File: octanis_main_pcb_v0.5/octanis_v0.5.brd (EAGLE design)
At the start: 80 x 45 mm, 78 parts, among them IC1 BME280, Q1 32.768kHz, Q2 32.768kHz, U3 DRV8836DSSR, U4 DRV8836DSSR, U5 DRV8836DSSR, U7 DRV8836DSSR

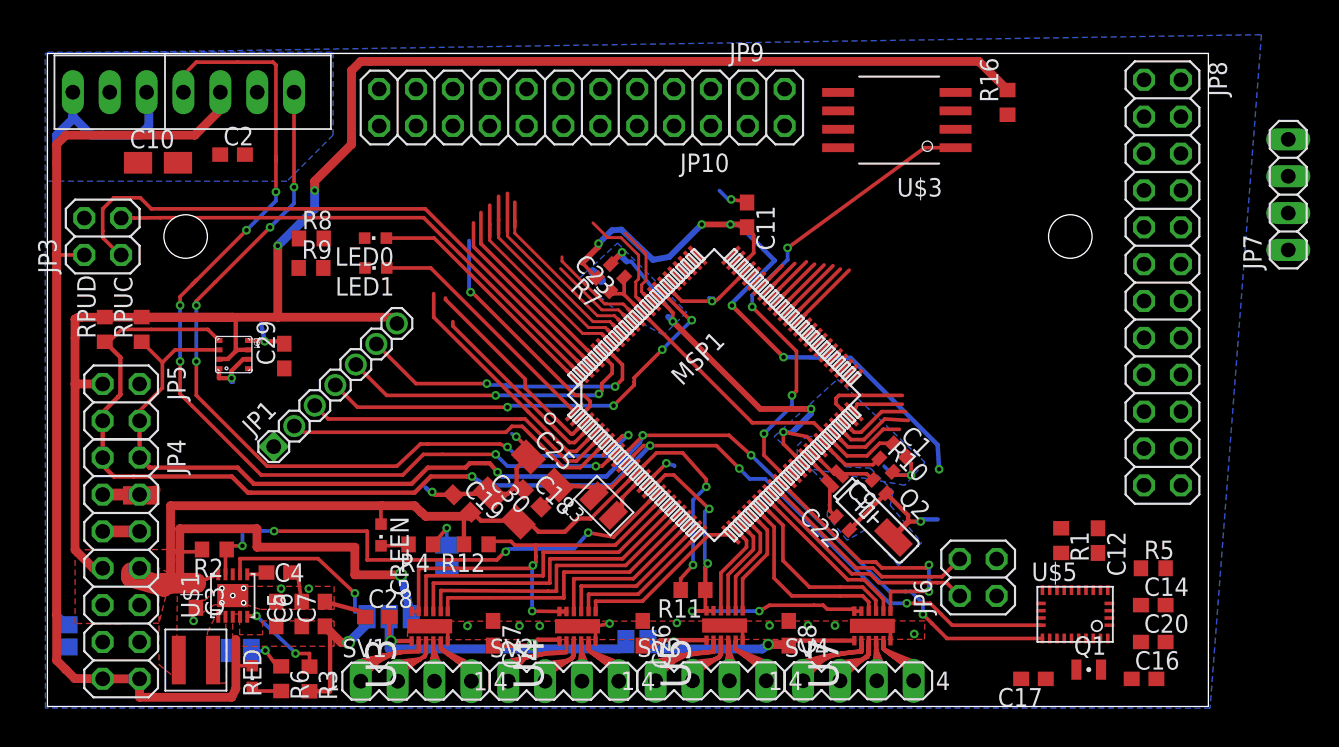
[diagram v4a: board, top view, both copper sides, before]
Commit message: mainboard: digital gpio routed
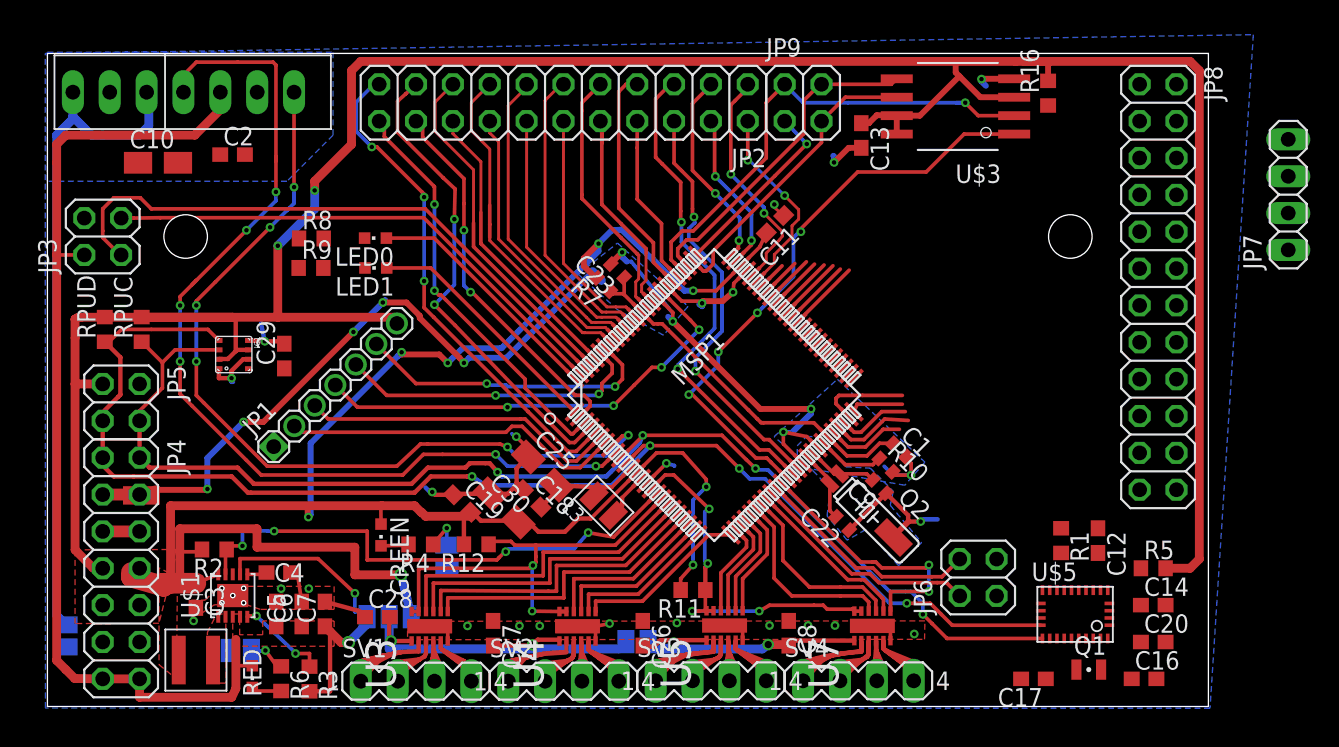
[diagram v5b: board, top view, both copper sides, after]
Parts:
- removed JP10: (no value), pinhead:2X10
- added C13: 100n, rcl:C0603
- added JP2: (no value), pinhead:2X11
- moved U$3 4.15 mm to (63.7, 41.3)
- moved R16 2.87 mm to (69.0, 42.3)
- moved JP9 2.56 mm to (52.1, 41.6)
- moved C11 2.03 mm to (50.1, 33.2), turned to 225 degrees
- moved JP8 0.43 mm to (76.5, 28.9)
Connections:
- removed net 3.3V: U$3.WP
- removed net N$15: JP10.2, MSP1.88
- removed net N$17: JP10.4, MSP1.89
- removed net N$20: JP10.6, MSP1.90
- removed net N$21: JP10.8, MSP1.91
- removed net P3.6/PM_UCB2SIMO/PM_UCB2SDA: MSP1.38
- removed net P3.7/PM_UCB2SOMI/PM_UCB2SCL: MSP1.39
- new net P3.6: JP2.5, MSP1.38
- new net P3.7: JP2.6, MSP1.39
- new net P7.0: JP2.12, MSP1.88
- new net P7.1: JP2.11, MSP1.89
- new net P7.2: JP2.14, MSP1.90
- new net P7.3: JP2.13, MSP1.91
- net +3V3: now also C13.1, U$3.WP
- net GND: now also C13.2
- net P1.0: now also JP2.19; no longer JP10.20
- net P1.1: now also JP2.21; no longer JP10.19
- net P10.2: now also JP2.20; no longer JP10.17
- net P10.3: now also JP2.22; no longer JP10.18
- net P5.6: now also JP2.2; no longer JP10.7
- net P5.7: now also JP2.1; no longer JP10.5
- net P6.6: now also JP2.8; no longer JP10.10
- net P6.7: now also JP2.7; no longer JP10.9
- net P9.2: now also JP2.4; no longer JP10.3
- net P9.3: now also JP2.3; no longer JP10.1
- net P9.4: now also JP2.18; no longer JP10.15
- net P9.5: now also JP2.17; no longer JP10.16
- net PJ.2: now also JP2.10; no longer JP10.13
- net PJ.3: now also JP2.9; no longer JP10.14
- net PJ.4: now also JP2.16; no longer JP10.11
- net PJ.5: now also JP2.15; no longer JP10.12
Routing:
- net +3V3: track 260.1 -> 331.1 mm, vias 11 -> 10
- net AGND: track 35.9 -> 77.4 mm, vias 5 -> 10
- net SPI_MISO: track 0.00 -> 34.3 mm, vias 0 -> 1
- net P3.6: track 0.00 -> 33.9 mm, vias 0 -> 2
- net P3.7: track 0.00 -> 29.9 mm, vias 0 -> 2
- net SPI_MOSI: track 0.00 -> 22.7 mm
- net P7.3: track 0.00 -> 21.6 mm
- net SPI_SCK: track 0.00 -> 20.7 mm
- net P7.1: track 0.00 -> 20.2 mm
- net P1.0: track 13.5 -> 33.1 mm, vias 0 -> 2
- net P7.2: track 0.00 -> 17.8 mm
- net P1.1: track 17.1 -> 34.8 mm, vias 0 -> 3
- net P7.0: track 0.00 -> 16.3 mm
- net P6.7: track 0.00 -> 16.0 mm
- net P5.7: track 0.00 -> 16.0 mm, vias 0 -> 2
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
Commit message: mainboard routing finished
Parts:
- removed JP7: SPI, pinhead:1X04
- moved C12 0.61 mm to (72.4, 10.8)
- moved R1 0.61 mm to (69.8, 10.8)
- moved R16 0.25 mm to (69.2, 42.3)
- moved C13 0.20 mm to (55.9, 39.3)
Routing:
- net +3V3: track 331.1 -> 369.3 mm
- net GND: track 72.2 -> 106.6 mm, vias 23 -> 32
- net A1: track 2.72 -> 34.1 mm
- net A0: track 1.99 -> 33.2 mm
- net A3: track 3.65 -> 33.1 mm
- net A9: track 0.00 -> 28.9 mm
- net A2: track 3.37 -> 30.3 mm
- net A8: track 0.00 -> 26.9 mm
- net A11: track 0.00 -> 26.8 mm
- net A5: track 4.47 -> 31.2 mm
- net A7: track 5.05 -> 31.2 mm
- net A13: track 0.00 -> 25.3 mm
- net A4: track 4.08 -> 28.9 mm
- net A17: track 0.00 -> 24.7 mm
- net A15: track 0.00 -> 24.7 mm
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
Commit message: mainboard finished
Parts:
- removed JP3: (no value), pinhead:2X02
- removed U$3: SST25VF064C, BertaLib:SOIC_8-LEAD
- added BLP, RST: PTR1B1,27, testpad:B1,27
- added RX3/TX3: (no value), pinhead:2X02
- added U6: DRV8836DSSR, DRV8834:SON50P200X300X80-13N
- U7: value DRV8836DSSR -> SST25VF064C; device DRV8834:SON50P200X300X80-13N -> BertaLib:SOIC_8-LEAD
- moved U7 36.4 mm to (63.7, 41.3)
- moved C11 1.15 mm to (50.0, 32.1)
- moved C2 0.57 mm to (12.7, 37.5)
- renumbered GREEN to 3V, JP1 to PROG, JP2 to DIGITAL_IO, JP6 to RX2/TX2, JP8 to ANALOG_IO, JP9 to SPI, L3 to L2, MSP1 to U1, RED to 5V, U$1 to U2, U$5 to IC2
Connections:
- removed net P5.6: DIGITAL_IO.2, U1.70
- removed net P5.7: DIGITAL_IO.1, U1.71
- net +3V3: now also DIGITAL_IO.1, RX2/TX2.3, RX3/TX3.3, U7.RST/HOLD, U7.VDD, U7.WP; no longer RX2/TX2.1, U$3.RST/HOLD, U$3.VDD, U$3.WP
- net +5V: no longer JP3.2
- net ACCEL_INT: now also U1.37
- net ACCEL_N_BOOTLD: now also BLP.TP
- net ACCEL_N_RST: now also RST.TP
- net GND: now also DIGITAL_IO.2, RX2/TX2.1, RX3/TX3.1, U1.71, U2.GND1, U2.GND2, U2.GND3, U2.GND4, U2.GND5, U6.13, U6.6, U7.VSS; no longer JP3.4, RX2/TX2.3, U$3.VSS, U7.13, U7.6
- net M5678SLEEP: now also U6.11, U6.12; no longer U7.11, U7.12
- net M7IN1: now also U6.10; no longer U7.10
- net M7IN2: now also U6.9; no longer U7.9
- net M8IN1: now also U6.8; no longer U7.8
- net M8IN2: now also U6.7; no longer U7.7
- net N$53: now also U6.2; no longer U7.2
- net N$54: now also U6.3; no longer U7.3
- net N$55: now also U6.4; no longer U7.4
- net N$56: now also U6.5; no longer U7.5
- net RX3: now also RX3/TX3.2; no longer JP3.1
- net SPI_FLASH_CS: now also U1.70, U7.CE; no longer U$3.CE, U1.37
- net SPI_MISO: now also U7.SO; no longer U$3.SO
- net SPI_MOSI: now also U7.SI; no longer U$3.SI
- net SPI_SCK: now also U7.SCK; no longer U$3.SCK
- net TX3: now also RX3/TX3.4; no longer JP3.3
- net V_MOTOR2: now also U6.1; no longer U7.1
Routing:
- net ACCEL_INT: track 0.00 -> 24.1 mm, vias 0 -> 2
- net P5.7: track 16.0 -> 0.00 mm, vias 2 -> 0
- net P5.6: track 13.7 -> 0.00 mm, vias 2 -> 0
- net SPI_FLASH_CS: track 41.5 -> 27.9 mm, vias 4 -> 0
- net GND: track 106.6 -> 114.6 mm
- net +3V3: track 369.3 -> 375.8 mm
- net TX3: track 36.0 -> 38.5 mm
- net ACCEL_N_RST: track 2.25 -> 4.41 mm
- net M7IN1: track 13.1 -> 11.0 mm
- net ACCEL_N_BOOTLD: track 4.25 -> 6.05 mm
- net +5V: track 98.1 -> 96.5 mm
- net RFGND: track 53.3 -> 54.9 mm
- net RX3: track 42.1 -> 43.7 mm
- net M7IN2: track 12.8 -> 11.4 mm
- net HX1_DATA: track 58.7 -> 59.5 mm
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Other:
- board text added: "A0 A1"
- board text added: "A22 A23"
- board text added: "CLK MOSI"
- board text added: "GND 3V3"
- board text added: "TE MISO"
- board text removed: "MISO MOSI TE CLK"

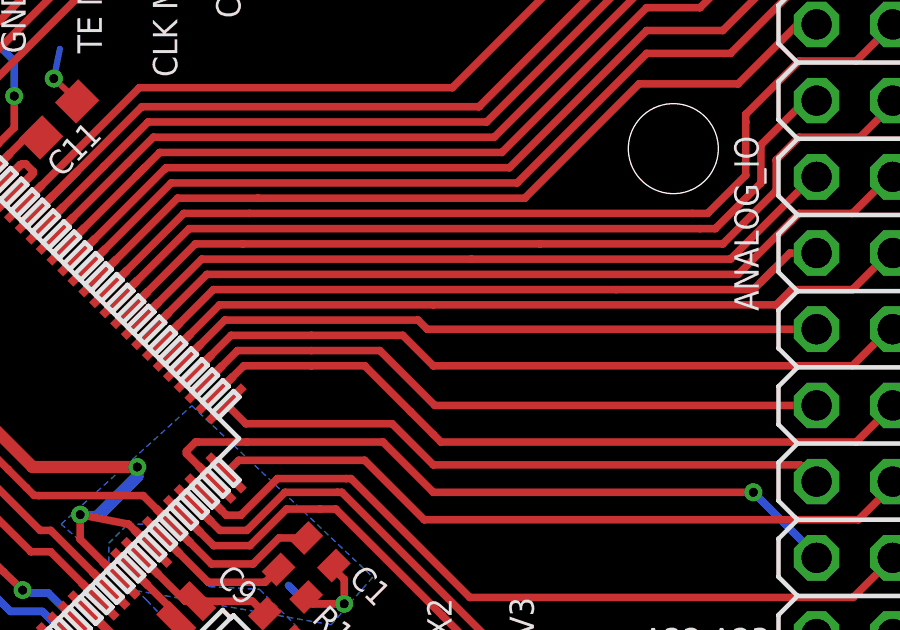
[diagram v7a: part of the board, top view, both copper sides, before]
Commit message: corrected UV sensor footprint
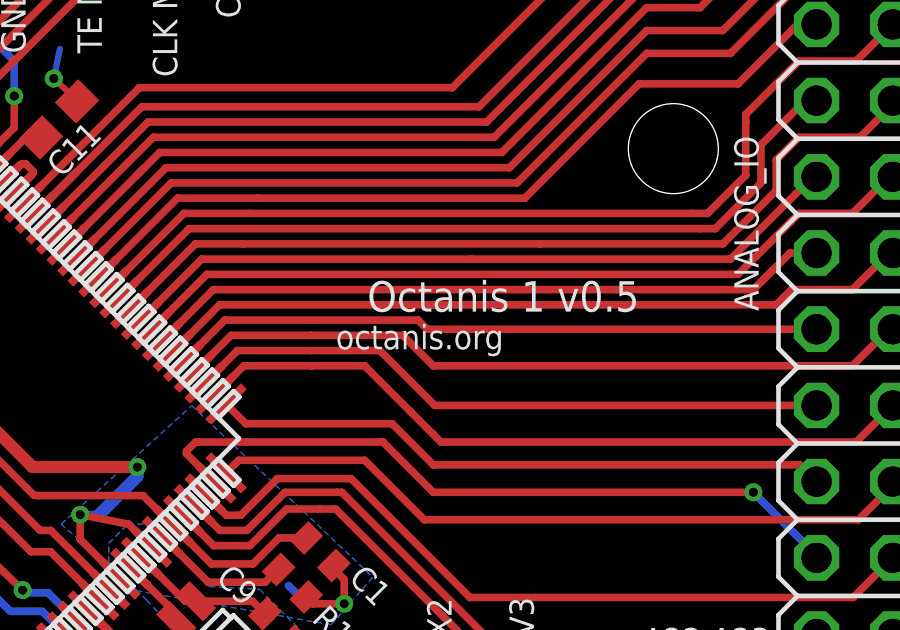
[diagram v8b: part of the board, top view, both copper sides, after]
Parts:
- renumbered SJ1 to VMOT_SEL, SJ2 to RF_J, SJ3 to LED_J2, SJ6 to MOT_J, SJ7 to LED_J1
